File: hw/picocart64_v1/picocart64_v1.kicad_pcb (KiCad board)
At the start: 4 copper layers, 100 x 60 mm, 21 parts, among them J1 USB_C_Receptacle_USB2.0, J2 Conn_01x05, Q1 BSS84, SW1 BootButton, U1 LY68L6400SLIT, U2 LY68L6400SLIT, U3 RP2040_Stamp, U4 N64-Cartridge

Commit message: hw: checkpoint
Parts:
- removed C1, C2: 100n, Capacitor_SMD:C_0603_1608Metric
- removed R4: 10k, Resistor_SMD:R_0603_1608Metric
- removed U1, U2: LY68L6400SLIT, Package_SO:SOIC-8_5.275x5.275mm_P1.27mm
- added J3: Conn_02x06_Odd_Even, Connector_PinSocket_2.54mm:PinSocket_2x06_P2.54mm_Horizontal, F.Cu at (196.8, 65.6)
- added J4: Micro_SD_Card_Det, Connector_Card:microSD_HC_Molex_104031-0811, F.Cu at (173.7, 67.3)
- moved SW1 53.5 mm to (132.1, 62.0), turned to 0 degrees
- moved J2 14.3 mm to (152.9, 62.5)
- moved JP1 9.08 mm to (176.8, 84.4)
- moved JP2 9.07 mm to (176.8, 81.8)
- moved JP3 9.04 mm to (176.8, 79.2)
- moved JP4 9.03 mm to (176.8, 76.7)
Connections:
- net /QSPI_RAM_CS0 renamed /PMOD_5_SIO2
- net /QSPI_RAM_CS1 renamed /PMOD_6_SIO3
- net /QSPI_RAM_IO0 renamed /PMOD_4_SCLK
- net /QSPI_RAM_SCK renamed /PMOD_1_SS
- U3 pad 28: /QSPI_RAM_IO1 -> /PMOD_2_SIO0
- U3 pad 29: /QSPI_RAM_IO2 -> /PMOD_3_SIO1
- U3 pad 30: /QSPI_RAM_IO3 -> /PMOD_7_CS0
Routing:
- net /PMOD_6_SIO3: track 16.6 -> 70.8 mm, vias 0 -> 2
- net /PMOD_3_SIO1: track 0.00 -> 44.1 mm, vias 0 -> 2
- net Net-(SW1-Pad2): track 47.2 -> 10.2 mm
- net /PMOD_2_SIO0: track 0.00 -> 36.6 mm, vias 0 -> 2
- net /QSPI_RAM_IO3: track 35.5 -> 0.00 mm, vias 2 -> 0
- net /PMOD_7_CS0: track 0.00 -> 33.4 mm, vias 0 -> 1
- net /PMOD_5_SIO2: track 29.4 -> 59.7 mm
- net /QSPI_RAM_IO1: track 30.0 -> 0.00 mm, vias 4 -> 0
- net /QSPI_RAM_IO2: track 28.5 -> 0.00 mm, vias 2 -> 0
- net /PMOD_4_SCLK: track 39.2 -> 58.7 mm
- net Net-(J1-PadS1): track 2.21 -> 19.2 mm
- net +3V3: track 141.4 -> 127.9 mm, vias 4 -> 2
- net /RP_SWDIO: track 33.5 -> 20.4 mm
- net /RP_SWDCLK: track 32.6 -> 19.5 mm
- net /~{RP_RESET}: track 31.7 -> 18.6 mm
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
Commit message: hw: PicoCart64 V1.0
First exploratory revision
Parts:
- U3: footprint RP2040_Stamp:RP2040_Stamp_SMD -> RP2040_Stamp:RP2040_Stamp_FlexyPin
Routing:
- net /N64_VCC: track 103.6 -> 96.4 mm
- net /AD0: track 73.8 -> 80.4 mm
- net /AD2: track 67.0 -> 73.4 mm
- net /N64_S_DAT: track 81.5 -> 87.7 mm
- net /N64_COLD_RESET: track 53.4 -> 58.6 mm
- net /USB_D+: track 49.8 -> 54.2 mm
- net /N64_CIC_DIO: track 43.9 -> 47.6 mm
- net Net-(SW1-Pad2): track 10.2 -> 13.6 mm
- net /AD9: track 31.0 -> 34.4 mm
- net /N64_NMI: track 74.6 -> 78.0 mm
- net /N64_CIC_DCLK: track 43.6 -> 46.9 mm
- net /N64_SI_CLK: track 67.8 -> 70.8 mm
- net /AD6: track 48.5 -> 51.3 mm
- net /USB_D-: track 50.1 -> 52.9 mm
- net /AD5: track 53.8 -> 56.3 mm
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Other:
- board text added: "+"
- board text added: "+3V3"
- board text added: "1. ~{SS}"
- board text added: "2. SIO0"
- board text added: "3. SIO1"
- board text added: "4. SCLK"
- board text added: "5. SIO2"
- board text added: "6. SIO3"
- board text added: "7. ~{CS0}"
- board text added: "8. N/C"
- board text added: "C"
- board text added: "D"
- board text added: "EEP_SDAT"
- board text added: "G"
- board text added: "GND"
- board text added: "NMI"
- board text added: "R"
- board text added: "SI_CLK"
- board text added: "SWCLK"
- board text added: "SWDIO"
- board text added: "S_DAT"
- board text added: "~{RST}"

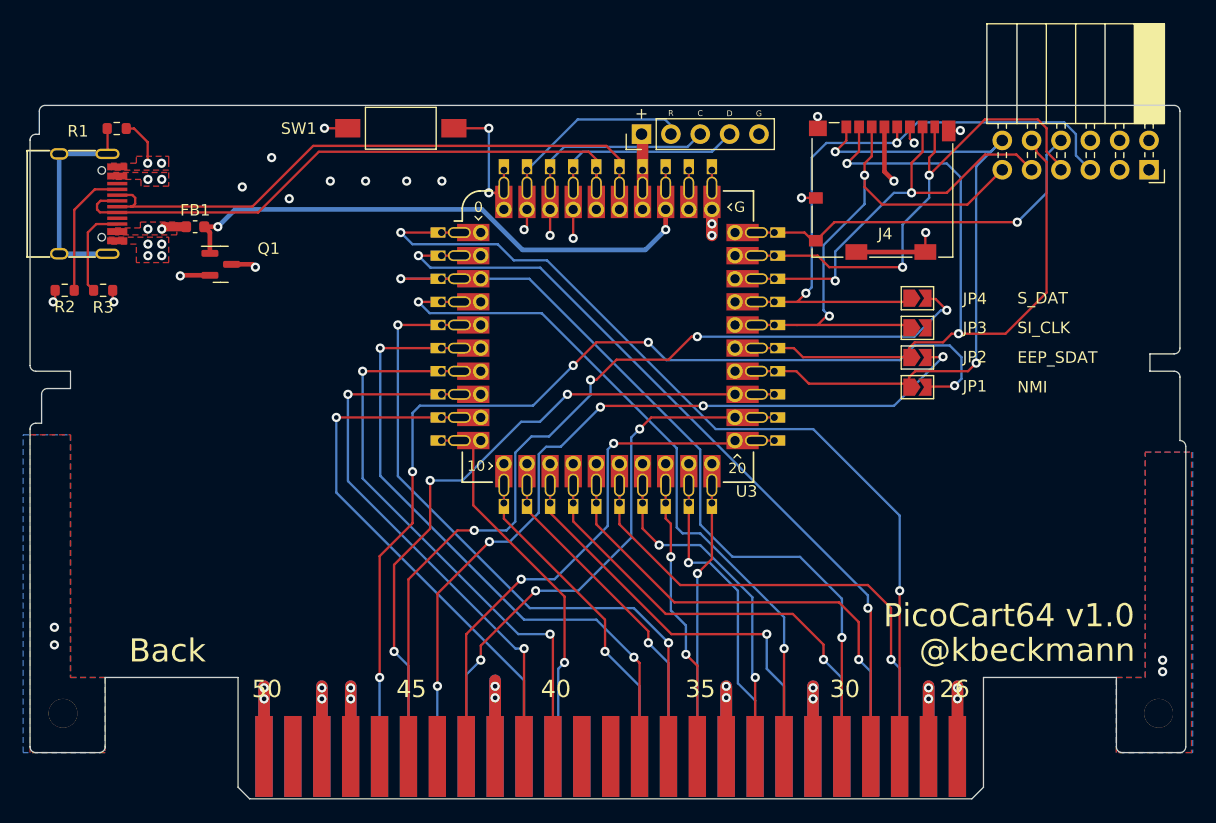
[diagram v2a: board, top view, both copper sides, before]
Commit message: hw: PicoCart64 V1.1
- KiCad project files
- Gerbers
- PDF
- Changelog since V1.0 + errata
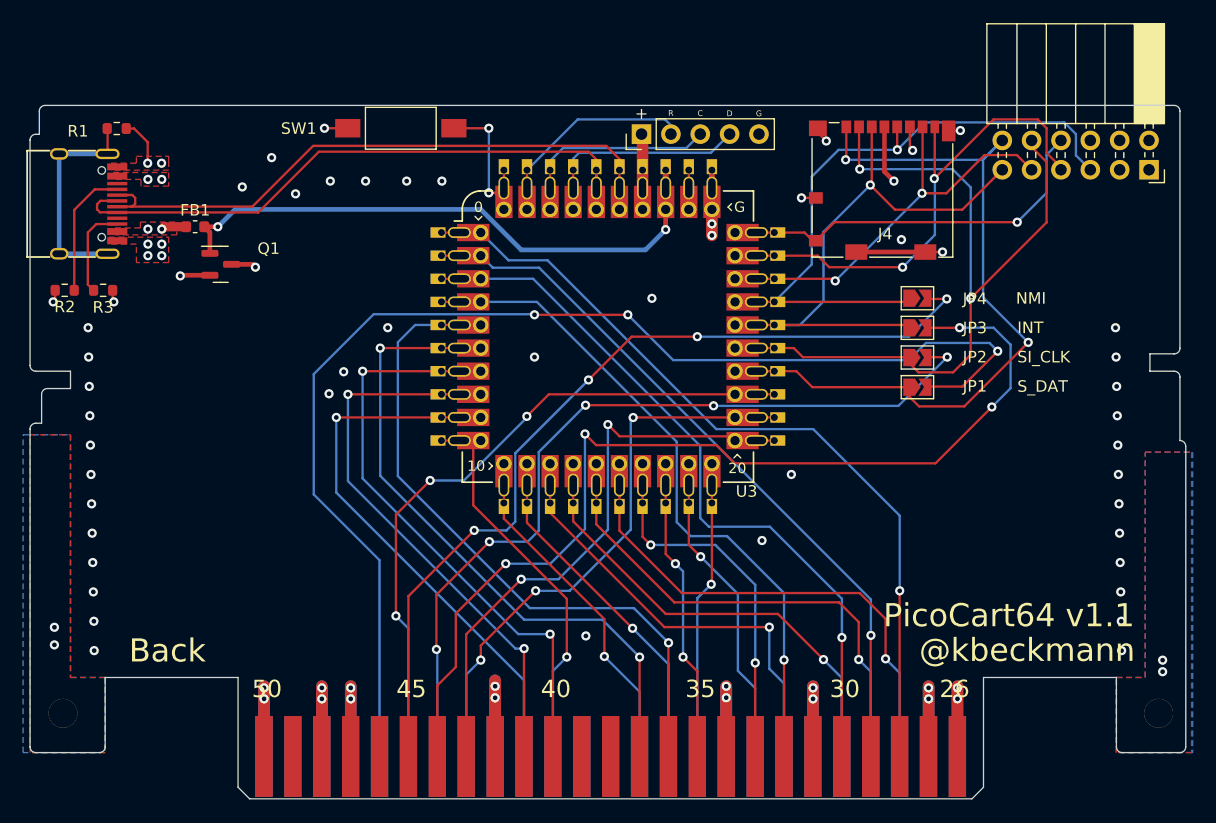
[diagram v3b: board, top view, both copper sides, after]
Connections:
- JP3 pad 2: /N64_EEP_SDAT -> /N64_INT
- U4 pad 44: unconnected-(U4-Pad44) -> /N64_INT
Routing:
- net /N64_INT: track 0.00 -> 87.7 mm, vias 0 -> 4
- net /N64_S_DAT: track 87.7 -> 106.8 mm, vias 5 -> 3
- net /AD2: track 73.4 -> 63.4 mm, vias 2 -> 1
- net /AD0: track 80.4 -> 70.6 mm, vias 2 -> 1
- net /AD1: track 69.9 -> 63.1 mm, vias 2 -> 1
- net /PMOD_5_SIO2: track 59.3 -> 65.6 mm
- net /AD3: track 63.8 -> 58.3 mm, vias 2 -> 1
- net /PMOD_6_SIO3: track 70.8 -> 66.8 mm
- net /RP_SWDIO: track 21.8 -> 18.8 mm, vias 1 -> 0
- net /RP_SWDCLK: track 21.0 -> 18.1 mm, vias 1 -> 0
- net /N64_CIC_DCLK: track 46.9 -> 49.4 mm
- net /~{RP_RESET}: track 21.1 -> 18.6 mm, vias 1 -> 0
- net /N64_SI_CLK: track 70.8 -> 72.6 mm
- net /PMOD_2_SIO0: track 37.8 -> 35.9 mm
- net /N64_NMI: track 78.0 -> 76.4 mm
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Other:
- board text added: "INT"
- board text removed: "EEP_SDAT"
